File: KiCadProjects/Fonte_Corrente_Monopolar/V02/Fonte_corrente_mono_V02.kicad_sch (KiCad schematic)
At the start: 31 parts, among them J1 alimentacao analogica, J2 sinais analogicos, J3 comunicacao / sinais digitais, J4 signal select, J7 Vref, U1-howland1 AD828AN, U2 INA128, U3-cond1 AD828AN

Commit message: Baseado barramento v04 - Finalizado - mudanca valor resitor leds
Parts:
- R13: value 390 -> 1.2k
- R7: value 360 -> 1.2k
- R8: value 160 -> 390
- R9: value 82 -> 240
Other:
- note added: "Iled => 5mA Vled ~ 3V"
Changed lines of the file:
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@@
+    (effects (font (size 1.27 1.27)) (justify left bottom))
+  )
+  (text "Iled => 5mA\nVled ~ 3V" (at 83.947 114.427 0)
     (effects (font (size 1.27 1.27)) (justify left bottom))
   )
@@
       (effects (font (size 1.27 1.27)) (justify left))
     )
-    (property "Value" "82" (at 76.2 116.967 0)
+    (property "Value" "240" (at 76.2 116.967 0)
       (effects (font (size 1.27 1.27)) (justify left))
     )
@@
       (effects (font (size 1.27 1.27)) (justify left))
     )
-    (property "Value" "390" (at 22.86 116.459 0)
+    (property "Value" "1.2k" (at 22.86 116.459 0)
       (effects (font (size 1.27 1.27)) (justify left))
     )
@@
       (effects (font (size 1.27 1.27)) (justify left))
     )
-    (property "Value" "360" (at 40.64 116.332 0)
+    (property "Value" "1.2k" (at 40.64 116.332 0)
       (effects (font (size 1.27 1.27)) (justify left))
     )
@@
       (effects (font (size 1.27 1.27)) (justify left))
     )
-    (property "Value" "160" (at 57.15 116.205 0)
-      (effects (font (size 1.27 1.27)) (justify left))
-    )
+    (property "Value" "390" (at 57.15 116.205 0)
+      (effects (font (size 1.27 1.27)) (justify left))
+    )

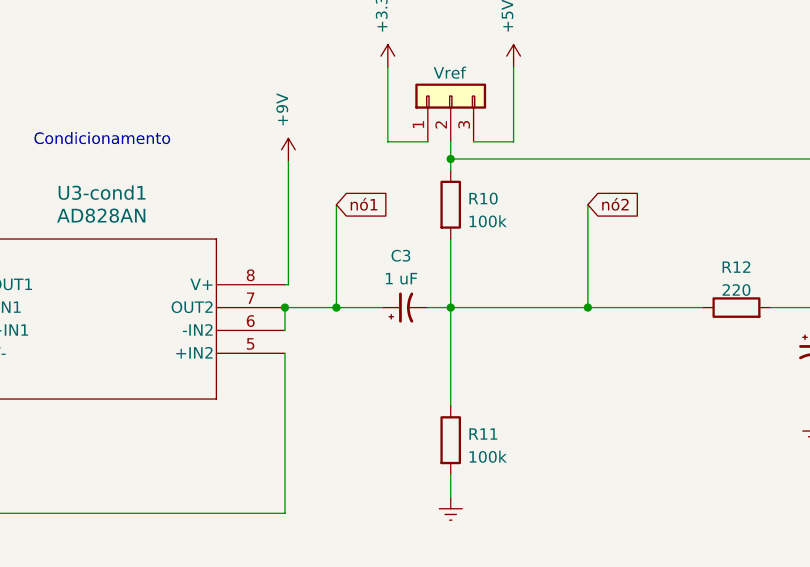
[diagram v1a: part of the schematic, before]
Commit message: Baseado barramento v04 - Finalizado - mudanca valor resitor leds
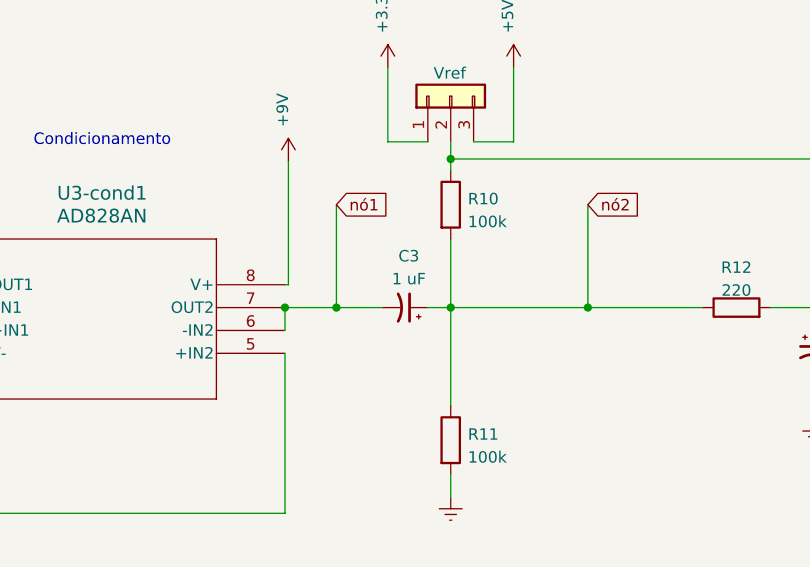
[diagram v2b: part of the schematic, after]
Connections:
- net nó1: now also C3.2; no longer C3.1
- net nó2: now also C3.1; no longer C3.2
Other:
- moved on the sheet: C3
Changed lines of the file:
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@@
     )
   )
-  (symbol (lib_id "Device:C_Polarized_Small_US") (at 172.72 119.38 90) (unit 1)
-    (in_bom yes) (on_board yes) (dnp no) (fields_autoplaced)
-    (property "Reference" "C3" (at 172.2882 113.665 90)
+  (symbol (lib_id "Device:C_Polarized_Small_US") (at 172.72 119.38 270) (mirror x) (unit 1)
+    (in_bom yes) (on_board yes) (dnp no)
+    (property "Reference" "C3" (at 173.1518 113.665 90)
       (effects (font (size 1.27 1.27)))
     )
-    (property "Value" "1 uF" (at 172.2882 116.205 90)
+    (property "Value" "1 uF" (at 173.1518 116.205 90)
       (effects (font (size 1.27 1.27)))
     )

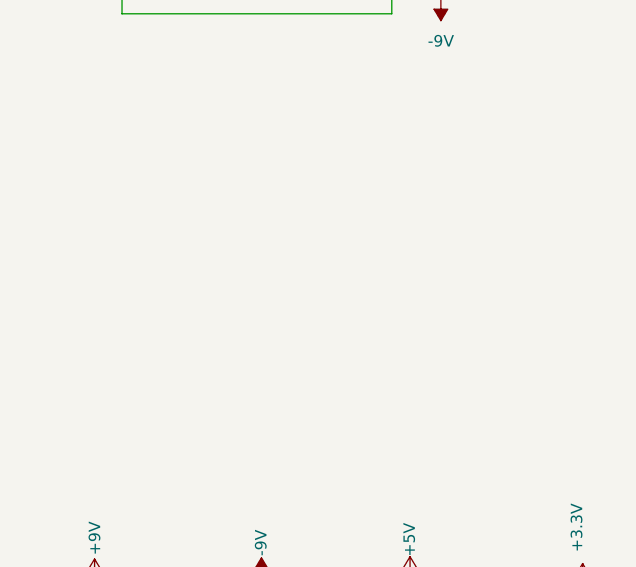
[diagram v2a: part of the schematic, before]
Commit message: Baseado barramento v04 - Finalizado - implementacao resistor pullup i2c 2
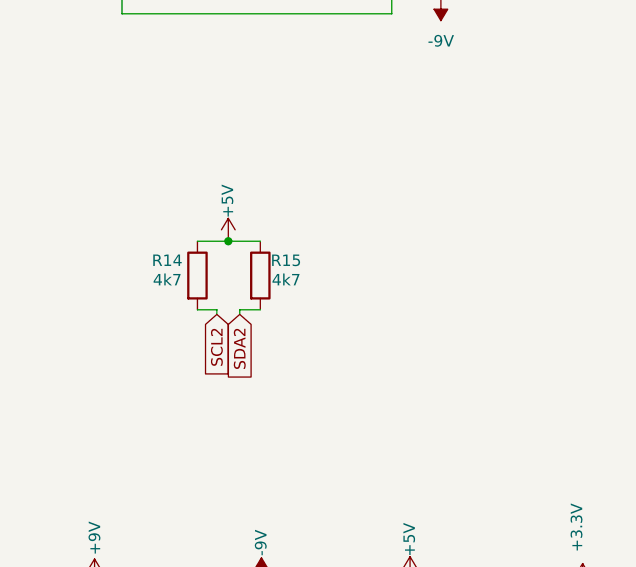
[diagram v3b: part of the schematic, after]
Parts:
- added R14, R15: 4k7, Resistor_THT:R_Axial_DIN0207_L6.3mm_D2.5mm_P7.62mm_Horizontal, symbol Device:R
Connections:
- net +5V: now also R14.1, R15.1
- net SCL2: now also R14.2
- net SDA2: now also R15.2
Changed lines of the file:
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@@
   (junction (at 154.686 182.499) (diameter 0) (color 0 0 0 0)
   )
+  (junction (at 34.798 73.533) (diameter 0) (color 0 0 0 0)
+  )
   (junction (at 41.6548 181.864) (diameter 0) (color 0 0 0 0)
   )
@@
     (stroke (width 0) (type default))
   )
+  (wire (pts (xy 38.354 73.533) (xy 34.798 73.533))
+    (stroke (width 0) (type default))
+  )
   (wire (pts (xy 99.06 68.58) (xy 99.06 69.85))
     (stroke (width 0) (type default))
@@
     (stroke (width 0) (type default))
   )
+  (wire (pts (xy 33.528 81.153) (xy 31.369 81.153))
+    (stroke (width 0) (type default))
+  )
   (wire (pts (xy 104.775 52.705) (xy 104.775 58.42))
     (stroke (width 0) (type default))
@@
     (stroke (width 0) (type default))
   )
+  (wire (pts (xy 36.068 81.153) (xy 38.354 81.153))
+    (stroke (width 0) (type default))
+  )
   (wire (pts (xy 28.575 40.64) (xy 28.575 44.45))
     (stroke (width 0) (type default))
@@
     (stroke (width 0) (type default))
   )
+  (wire (pts (xy 34.798 73.533) (xy 31.369 73.533))
+    (stroke (width 0) (type default))
+  )
   (wire (pts (xy 19.177 141.859) (xy 19.177 152.019))
     (stroke (width 0) (type default))
@@
     (stroke (width 0) (type default))
   )
+  (wire (pts (xy 36.068 81.661) (xy 36.068 81.153))
+    (stroke (width 0) (type default))
+  )
   (wire (pts (xy 58.42 15.875) (xy 58.42 33.02))
     (stroke (width 0) (type default))
@@
   )
   (wire (pts (xy 159.766 116.84) (xy 159.385 116.84))
+    (stroke (width 0) (type default))
+  )
+  (wire (pts (xy 33.528 81.661) (xy 33.528 81.153))
     (stroke (width 0) (type default))
   )
@@
     )
   )
+  (global_label "SDA2" (shape input) (at 36.068 81.661 270) (fields_autoplaced)
+    (effects (font (size 1.27 1.27)) (justify right))
+    (property "Intersheetrefs" "${INTERSHEET_REFS}" (at 36.068 89.4238 90)
+      (effects (font (size 1.27 1.27)) (justify right) hide)
+    )
+  )
   (global_label "I1" (shape input) (at 57.277 152.019 90) (fields_autoplaced)
     (effects (font (size 1.27 1.27)) (justify left))
@@
     (property "Intersheetrefs" "${INTERSHEET_REFS}" (at 246.7459 45.72 0)
       (effects (font (size 1.27 1.27)) (justify left) hide)
+    )
+  )
+  (global_label "SCL2" (shape input) (at 33.528 81.661 270) (fields_autoplaced)
+    (effects (font (size 1.27 1.27)) (justify right))
+    (property "Intersheetrefs" "${INTERSHEET_REFS}" (at 33.528 89.3633 90)
+      (effects (font (size 1.27 1.27)) (justify right) hide)
     )
   )
@@
     )
   )
+  (symbol (lib_id "Device:R") (at 31.369 77.343 0) (unit 1)
+    (in_bom yes) (on_board yes) (dnp no)
+    (property "Reference" "R14" (at 26.289 75.692 0)
+      (effects (font (size 1.27 1.27)) (justify left))
+    )
+    (property "Value" "4k7" (at 26.416 77.851 0)
+      (effects (font (size 1.27 1.27)) (justify left))
+    )
+    (property "Footprint" "Resistor_THT:R_Axial_DIN0207_L6.3mm_D2.5mm_P7.62mm_Horizontal" (at 29.591 77.343 90)
+      (effects (font (size 1.27 1.27)) hide)
+    )
+    (property "Datasheet" "~" (at 31.369 77.343 0)
+      (effects (font (size 1.27 1.27)) hide)
+    )
+    (pin "1")
+    (pin "2")
+    (instances
+      (project "Fonte_corrente_mono_V02"
+        (path "/f0ff92cf-26e5-4ab9-977d-5f9689e8a5d0"
+          (reference "R14") (unit 1)
+        )
+      )
+    )
+  )
   (symbol (lib_id "power:Earth") (at 24.257 141.859 180) (unit 1)
     (in_bom yes) (on_board yes) (dnp no) (fields_autoplaced)
@@
         (path "/f0ff92cf-26e5-4ab9-977d-5f9689e8a5d0"
           (reference "R8") (unit 1)
+        )
+      )
+    )
+  )
+  (symbol (lib_id "Device:R") (at 38.354 77.343 0) (unit 1)
+    (in_bom yes) (on_board yes) (dnp no)
+    (property "Reference" "R15" (at 39.497 75.692 0)
+      (effects (font (size 1.27 1.27)) (justify left))
+    )
+    (property "Value" "4k7" (at 39.624 77.851 0)
+      (effects (font (size 1.27 1.27)) (justify left))
+    )
+    (property "Footprint" "Resistor_THT:R_Axial_DIN0207_L6.3mm_D2.5mm_P7.62mm_Horizontal" (at 36.576 77.343 90)
+      (effects (font (size 1.27 1.27)) hide)
+    )
+    (property "Datasheet" "~" (at 38.354 77.343 0)
+      (effects (font (size 1.27 1.27)) hide)
+    )
+    (pin "2")
+    (pin "1")
+    (instances
+      (project "Fonte_corrente_mono_V02"
+        (path "/f0ff92cf-26e5-4ab9-977d-5f9689e8a5d0"
+          (reference "R15") (unit 1)
         )
       )
@@
         )
       )
+    )
+  )
+  (symbol (lib_id "power:+5V") (at 34.798 73.533 0) (unit 1)
+    (in_bom yes) (on_board yes) (dnp no)
+    (property "Reference" "#PWR054" (at 34.798 77.343 0)
+      (effects (font (size 1.27 1.27)) hide)
+    )
+    (property "Value" "+5V" (at 34.7439 70.9845 90)
+      (effects (font (size 1.27 1.27)) (justify left))
+    )
+    (property "Footprint" "" (at 34.798 73.533 0)
+      (effects (font (size 1.27 1.27)) hide)
+    )
+    (property "Datasheet" "" (at 34.798 73.533 0)
+      (effects (font (size 1.27 1.27)) hide)
+    )
+    (pin "1")
+    (instances
+      (project "Fonte_corrente_mono_V02"
+        (path "/f0ff92cf-26e5-4ab9-977d-5f9689e8a5d0"
+          (reference "#PWR054") (unit 1)
+        )
+      )

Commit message: Baseado barramento v04 - Finalizado
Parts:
- J7: value Vref -> +3.3V | +5.0V
- renumbered D5 to L+3.3v1, D4 to L+5v1, D6 to L+9v1, D3 to L-9v1, RganhoINA1 to Rganho-I1, R14 to RpSCL2, R15 to RpSDA2, Rsentinela1 to Rsentinela-I1, U2 to U2-INA-I1
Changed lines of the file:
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@@
   (symbol (lib_id "Device:LED") (at 54.991 122.555 90) (unit 1)
     (in_bom yes) (on_board yes) (dnp no) (fields_autoplaced)
-    (property "Reference" "D4" (at 58.42 122.8725 90)
+    (property "Reference" "L+5v1" (at 58.42 122.8725 90)
       (effects (font (size 1.27 1.27)) (justify right))
     )
@@
       (project "Fonte_corrente_mono_V02"
         (path "/f0ff92cf-26e5-4ab9-977d-5f9689e8a5d0"
-          (reference "D4") (unit 1)
+          (reference "L+5v1") (unit 1)
         )
       )
@@
   (symbol (lib_id "Amplifier_Instrumentation:INA128") (at 211.455 45.72 0) (unit 1)
     (in_bom yes) (on_board yes) (dnp no)
-    (property "Reference" "U2" (at 218.059 36.576 0)
+    (property "Reference" "U2-INA-I1" (at 218.059 36.576 0)
       (effects (font (size 1.27 1.27)))
     )
@@
       (project "Fonte_corrente_mono_V02"
         (path "/f0ff92cf-26e5-4ab9-977d-5f9689e8a5d0"
-          (reference "U2") (unit 1)
+          (reference "U2-INA-I1") (unit 1)
         )
       )
@@
   (symbol (lib_id "Device:R") (at 195.58 45.72 0) (unit 1)
     (in_bom yes) (on_board yes) (dnp no) (fields_autoplaced)
-    (property "Reference" "RganhoINA1" (at 198.12 44.45 0)
+    (property "Reference" "Rganho-I1" (at 198.12 44.45 0)
       (effects (font (size 1.27 1.27)) (justify left))
     )
@@
       (project "Fonte_corrente_mono_V02"
         (path "/f0ff92cf-26e5-4ab9-977d-5f9689e8a5d0"
-          (reference "RganhoINA1") (unit 1)
+          (reference "Rganho-I1") (unit 1)
         )
       )
@@
   (symbol (lib_id "Device:R") (at 183.515 45.72 0) (unit 1)
     (in_bom yes) (on_board yes) (dnp no) (fields_autoplaced)
-    (property "Reference" "Rsentinela1" (at 185.42 44.45 0)
+    (property "Reference" "Rsentinela-I1" (at 185.42 44.45 0)
       (effects (font (size 1.27 1.27)) (justify left))
     )
@@
       (project "Fonte_corrente_mono_V02"
         (path "/f0ff92cf-26e5-4ab9-977d-5f9689e8a5d0"
-          (reference "Rsentinela1") (unit 1)
+          (reference "Rsentinela-I1") (unit 1)
         )
       )
@@
   (symbol (lib_id "Device:LED") (at 38.481 122.682 270) (unit 1)
     (in_bom yes) (on_board yes) (dnp no) (fields_autoplaced)
-    (property "Reference" "D3" (at 40.64 119.8245 90)
+    (property "Reference" "L-9v1" (at 40.64 119.8245 90)
       (effects (font (size 1.27 1.27)) (justify left))
     )
@@
       (project "Fonte_corrente_mono_V02"
         (path "/f0ff92cf-26e5-4ab9-977d-5f9689e8a5d0"
-          (reference "D3") (unit 1)
+          (reference "L-9v1") (unit 1)
         )
       )
@@
       (effects (font (size 1.27 1.27)) (justify left) hide)
     )
-    (property "Value" "Vref" (at 175.895 93.345 90)
+    (property "Value" "+3.3V | +5.0V" (at 170.307 92.71 90)
       (effects (font (size 1.27 1.27)) (justify right))
     )
@@
   (symbol (lib_id "Device:R") (at 31.369 77.343 0) (unit 1)
     (in_bom yes) (on_board yes) (dnp no)
-    (property "Reference" "R14" (at 26.289 75.692 0)
+    (property "Reference" "RpSCL2" (at 26.289 75.692 0)
       (effects (font (size 1.27 1.27)) (justify left))
     )
@@
       (project "Fonte_corrente_mono_V02"
         (path "/f0ff92cf-26e5-4ab9-977d-5f9689e8a5d0"
-          (reference "R14") (unit 1)
+          (reference "RpSCL2") (unit 1)
         )
       )
@@
   (symbol (lib_id "Device:LED") (at 74.168 123.317 90) (unit 1)
     (in_bom yes) (on_board yes) (dnp no) (fields_autoplaced)
-    (property "Reference" "D5" (at 77.47 123.6345 90)
+    (property "Reference" "L+3.3v1" (at 77.47 123.6345 90)
       (effects (font (size 1.27 1.27)) (justify right))
     )
@@
       (project "Fonte_corrente_mono_V02"
         (path "/f0ff92cf-26e5-4ab9-977d-5f9689e8a5d0"
-          (reference "D5") (unit 1)
+          (reference "L+3.3v1") (unit 1)
         )
       )
@@
   (symbol (lib_id "Device:LED") (at 19.939 122.809 90) (unit 1)
     (in_bom yes) (on_board yes) (dnp no) (fields_autoplaced)
-    (property "Reference" "D6" (at 23.241 123.1265 90)
+    (property "Reference" "L+9v1" (at 22.86 123.1265 90)
       (effects (font (size 1.27 1.27)) (justify right))
     )
-    (property "Value" "LED - Blue" (at 23.241 125.6665 90)
+    (property "Value" "LED - Blue" (at 22.86 125.6665 90)
       (effects (font (size 1.27 1.27)) (justify right))
     )
@@
       (project "Fonte_corrente_mono_V02"
         (path "/f0ff92cf-26e5-4ab9-977d-5f9689e8a5d0"
-          (reference "D6") (unit 1)
+          (reference "L+9v1") (unit 1)
         )
       )
@@
   (symbol (lib_id "Device:R") (at 38.354 77.343 0) (unit 1)
     (in_bom yes) (on_board yes) (dnp no)
-    (property "Reference" "R15" (at 39.497 75.692 0)
+    (property "Reference" "RpSDA2" (at 39.497 75.692 0)
       (effects (font (size 1.27 1.27)) (justify left))
     )
@@
       (project "Fonte_corrente_mono_V02"
         (path "/f0ff92cf-26e5-4ab9-977d-5f9689e8a5d0"
-          (reference "R15") (unit 1)
-        )
-      )
+          (reference "RpSDA2") (unit 1)
+        )
+      )

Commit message: temp
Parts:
- added RpSCL1, RpSCL3, RpSCL4, RpSDA1, RpSDA3, RpSDA4: 4k7, Resistor_THT:R_Axial_DIN0207_L6.3mm_D2.5mm_P7.62mm_Horizontal, symbol Device:R
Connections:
- net +3.3V: now also RpSCL1.2, RpSCL3.2, RpSDA1.2, RpSDA3.2
- net +5V: now also RpSCL4.1, RpSDA4.1
- net SCL1: now also RpSCL1.1
- net SCL3: now also RpSCL3.1
- net SCL4: now also RpSCL4.2
- net SDA1: now also RpSDA1.1
- net SDA3: now also RpSDA3.1
- net SDA4: now also RpSDA4.2
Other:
- moved on the sheet: RpSCL2, RpSDA2
